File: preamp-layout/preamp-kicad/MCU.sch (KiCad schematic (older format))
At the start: 9 parts, among them J27 Conn_01x04_Female, J29 Conn_01x05_Female, J30 Conn_01x05_Female, J31 Conn_01x05_Female, J32 Conn_01x04_Female, J33 Conn_01x03_Male, J34 Conn_01x02_Male, J35 Conn_01x02_Male, U5 ESP32-DevKitC

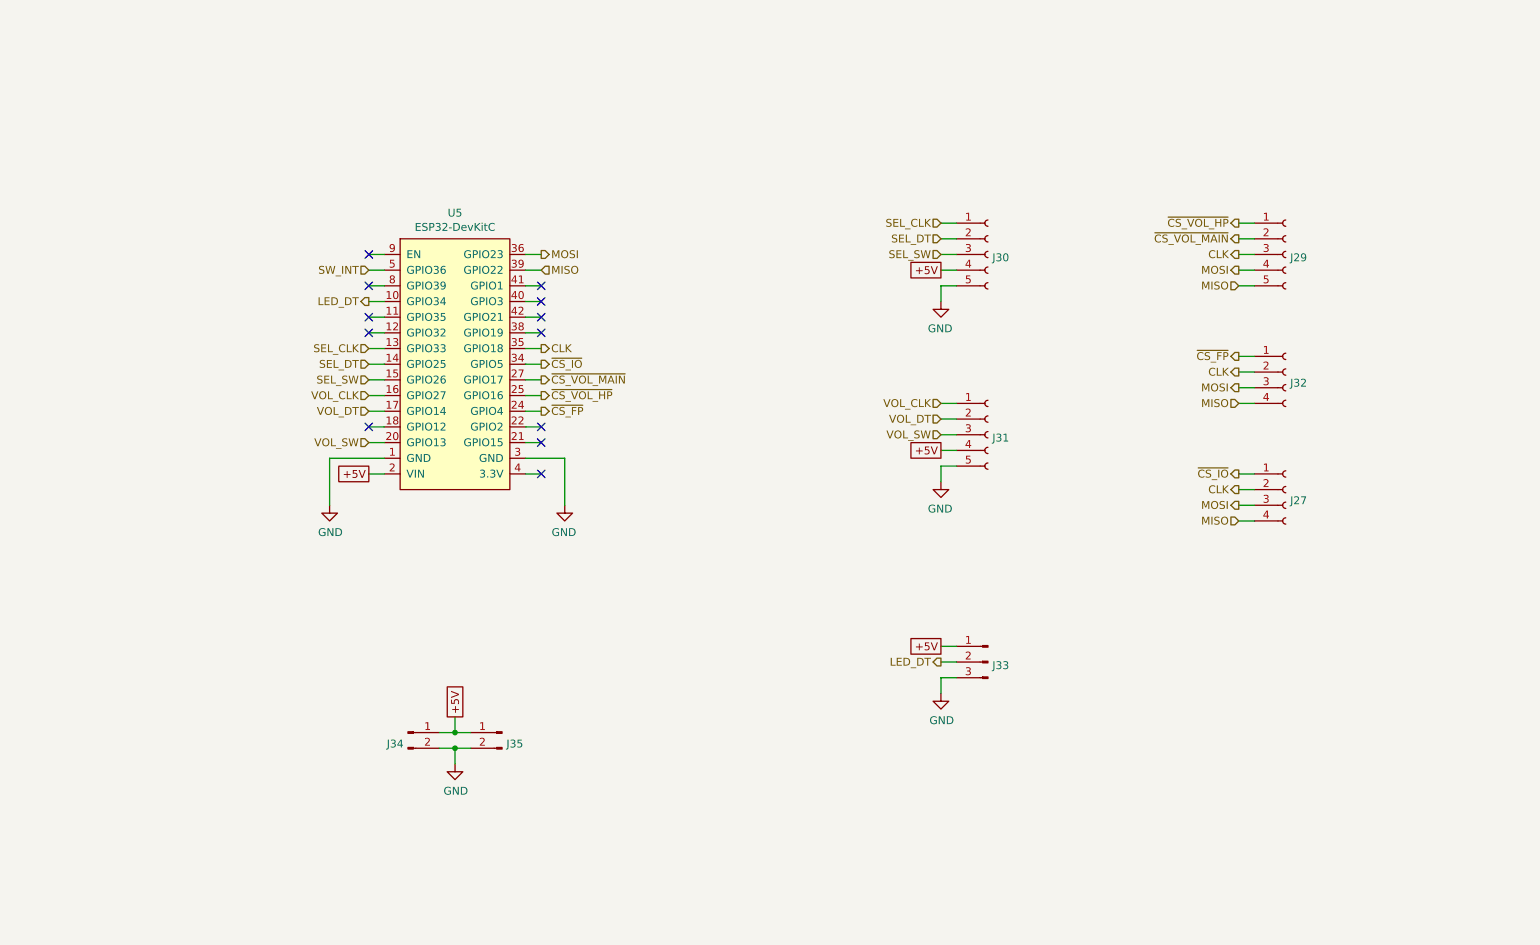
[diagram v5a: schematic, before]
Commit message: I2C init commit
Changed design from using SPI interface to I2C interface, with exception of front LED array (SPI).
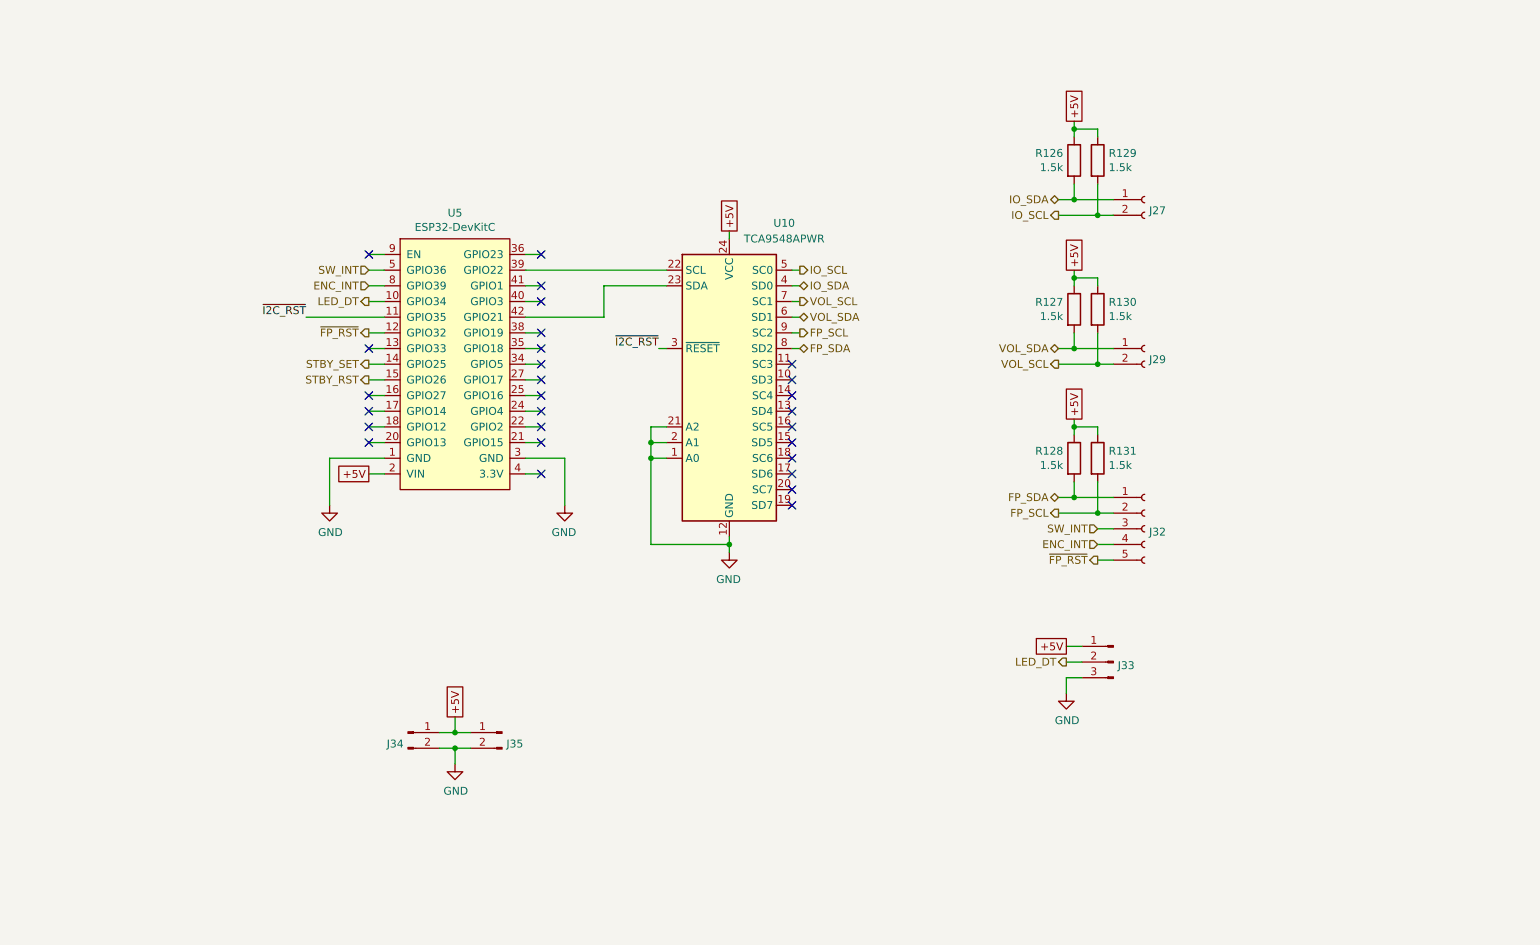
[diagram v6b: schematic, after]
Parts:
- removed J27, J32: Conn_01x04_Female, symbol Connector:Conn_01x04_Female
- removed J29, J30, J31: Conn_01x05_Female, symbol Connector:Conn_01x05_Female
- added J27, J29: Conn_01x02_Female, symbol Connector:Conn_01x02_Female
- added J32: Conn_01x05_Female, symbol Connector:Conn_01x05_Female
- added R126, R127, R128, R129, R130, R131: 1.5k, symbol Device:R
- added U10: TCA9548APWR, Package_SO:TSSOP-24_4.4x7.8mm_P0.65mm, symbol Interface_Expansion:TCA9548APWR
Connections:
- net +5V: now also R126.1, R127.1, R128.1, R129.1, R130.1, R131.1, U10.24 (VCC)
- net GND: now also U10.1 (A0), U10.12 (GND), U10.2 (A1), U10.21 (A2)
- net SW_INT: now also J32.3 (Pin_3)
- net ~I2C_RST: now reaches U5.11 (GPIO35)
- net ~I2C_RST: now also U10.3 (~RESET)
- net ~FP_RST: now reaches U5.12 (GPIO32)
- net ~FP_RST: now also J32.5 (Pin_5)
- net at U5.42 (GPIO21): now also U10.23 (SDA)
- net ENC_INT: now reaches U5.8 (GPIO39)
- net ENC_INT: now also J32.4 (Pin_4)
- net CLK: no longer names the net of U5.35 (GPIO18)
- net MISO: no longer names the net of U5.39 (GPIO22)
- net MISO: now also U10.22 (SCL)
- net MOSI: no longer names the net of U5.36 (GPIO23)
- net SEL_CLK: no longer names the net of U5.13 (GPIO33)
- net SEL_DT renamed STBY_SET
- net SEL_SW renamed STBY_RST
- net VOL_CLK: no longer names the net of U5.16 (GPIO27)
- net VOL_DT: no longer names the net of U5.17 (GPIO14)
- net VOL_SW: no longer names the net of U5.20 (GPIO13)
- net ~CS_FP: no longer names the net of U5.24 (GPIO4)
- net ~CS_IO: no longer names the net of U5.34 (GPIO5)
- net ~CS_VOL_HP: no longer names the net of U5.25 (GPIO16)
- net ~CS_VOL_MAIN: no longer names the net of U5.27 (GPIO17)
- new net FP_SCL: J32.2 (Pin_2), R131.2, U10.9 (SC2)
- new net FP_SDA: J32.1 (Pin_1), R128.2, U10.8 (SD2)
- new net IO_SCL: J27.2 (Pin_2), R129.2, U10.5 (SC0)
- new net IO_SDA: J27.1 (Pin_1), R126.2, U10.4 (SD0)
- new net VOL_SCL: J29.2 (Pin_2), R130.2, U10.7 (SC1)
- new net VOL_SDA: J29.1 (Pin_1), R127.2, U10.6 (SD1)
- no-connect marks 12 -> 28
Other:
- moved on the sheet: J33

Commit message: BOM Update
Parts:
- added J28, J30: Conn_01x15_Female, symbol Connector:Conn_01x15_Female
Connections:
- net +5V: now also J28.15 (Pin_15); no longer U5.2 (VIN)
- net ENC_INT: now also J28.3 (Pin_3); no longer U5.8 (GPIO39)
- net GND: now also J28.14 (Pin_14), J30.14 (Pin_14); no longer U5.1 (GND), U5.3 (GND)
- net LED_DT: now also J28.4 (Pin_4); no longer U5.10 (GPIO34)
- net STBY_RST: now also J28.9 (Pin_9); no longer U5.15 (GPIO26)
- net STBY_SET: now also J28.8 (Pin_8); no longer U5.14 (GPIO25)
- net SW_INT: now also J28.2 (Pin_2); no longer U5.5 (GPIO36)
- net ~FP_RST: now also J28.6 (Pin_6); no longer U5.12 (GPIO32)
- net ~I2C_RST: now also J28.5 (Pin_5); no longer U5.11 (GPIO35)
- net at U10.22 (SCL): now also J30.2 (Pin_2); no longer U5.39 (GPIO22)
- net at U10.23 (SDA): now also J30.5 (Pin_5); no longer U5.42 (GPIO21)
- no-connect marks 28 -> 58
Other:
- moved on the sheet: J27, J29, J32, J33, J34, J35, R126, R127, R128, R129, R130, R131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

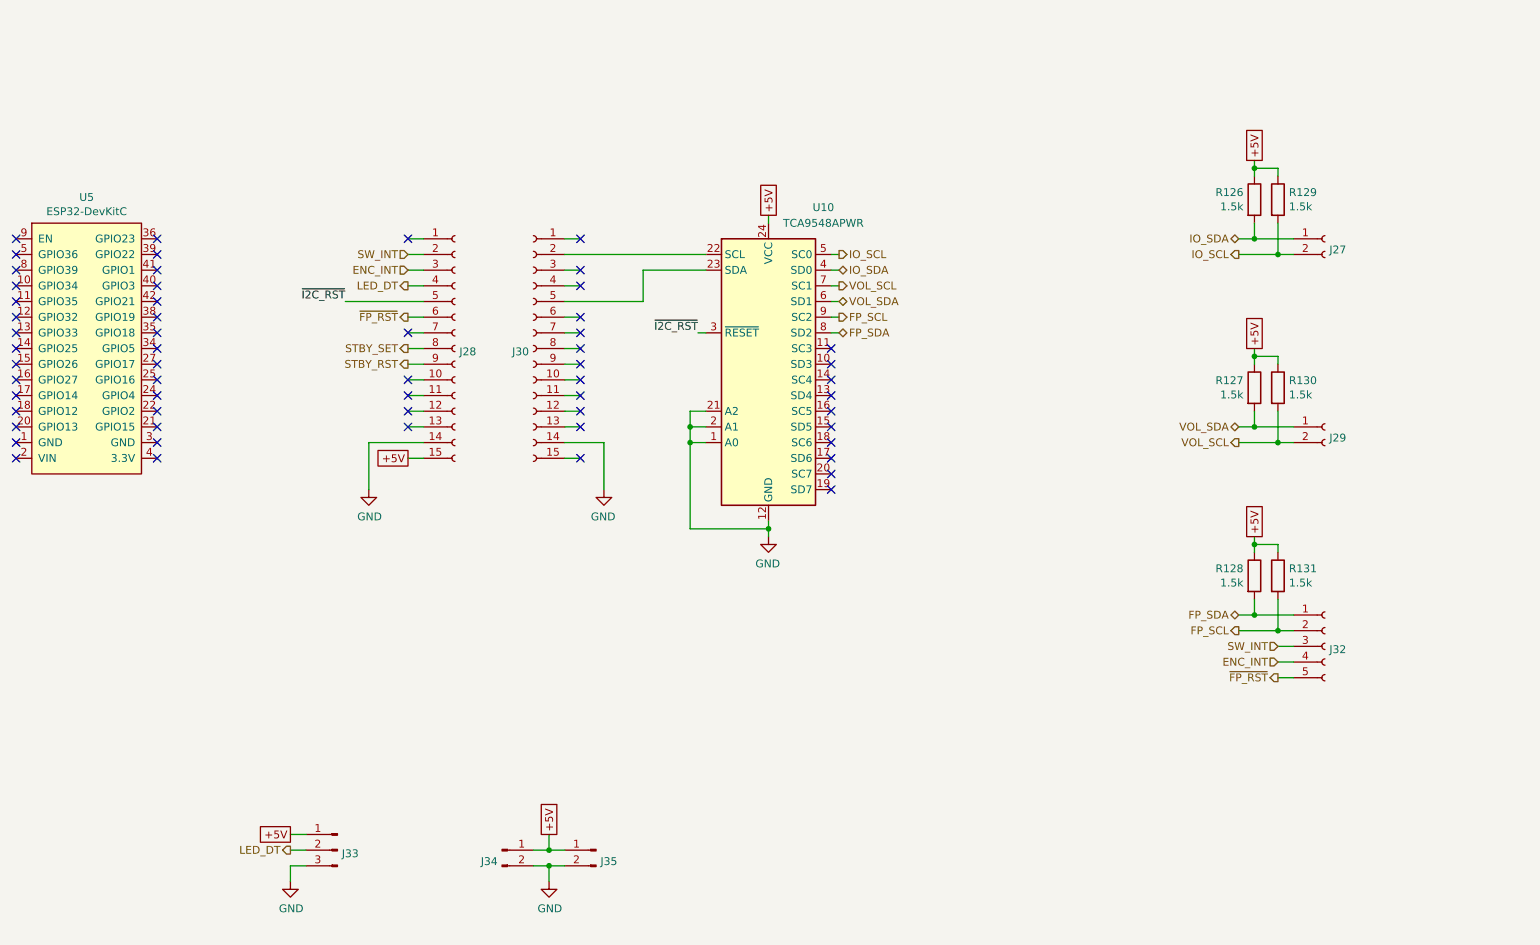
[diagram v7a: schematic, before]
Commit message: woops
to merge with I2C
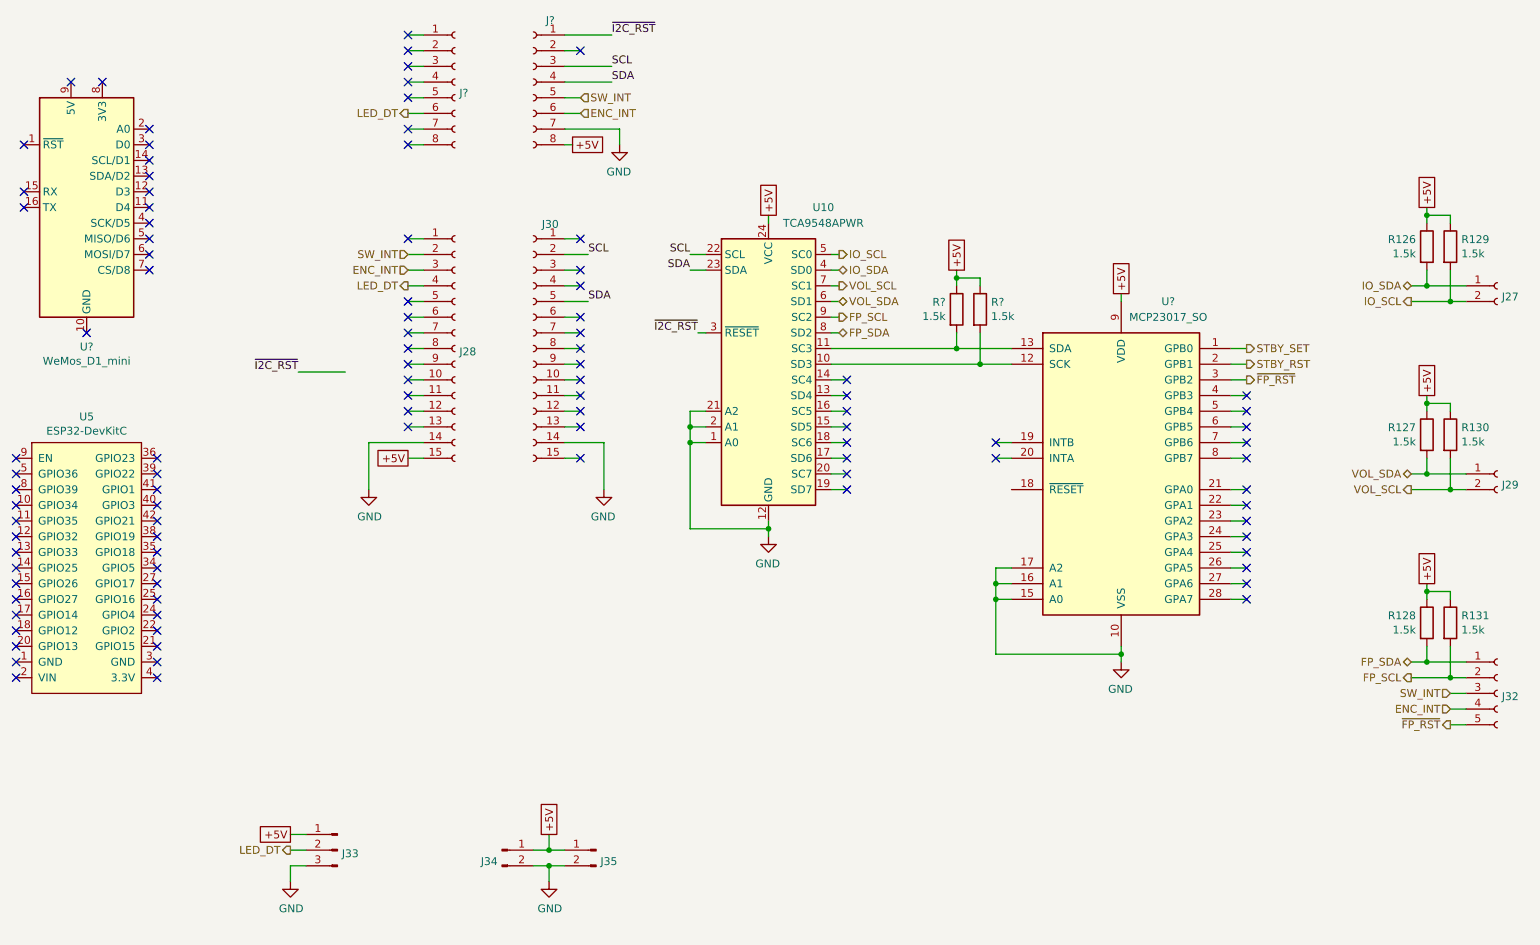
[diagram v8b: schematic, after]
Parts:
- added J? (x2): Conn_01x08_Female, symbol Connector:Conn_01x08_Female
- added R? (x2): 1.5k, symbol Device:R
- added U?: WeMos_D1_mini, Module:WEMOS_D1_mini_light, symbol MCU_Module:WeMos_D1_mini
- added U?: MCP23017_SO, Package_SO:SOIC-28W_7.5x17.9mm_P1.27mm, symbol Interface_Expansion:MCP23017_SO
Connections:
- net +5V: now also J?.8 (Pin_8), R?.1, R?.1, U?.9 (VDD)
- net ENC_INT: now also J?.6 (Pin_6)
- net GND: now also J?.7 (Pin_7), U?.10 (VSS), U?.15 (A0), U?.16 (A1), U?.17 (A2)
- net LED_DT: now also J?.6 (Pin_6)
- net STBY_RST: now also U?.2 (GPB1); no longer J28.9 (Pin_9)
- net STBY_SET: now also U?.1 (GPB0); no longer J28.8 (Pin_8)
- net SW_INT: now also J?.5 (Pin_5)
- net ~FP_RST: now also U?.3 (GPB2); no longer J28.6 (Pin_6)
- net ~I2C_RST: now also J?.1 (Pin_1); no longer J28.5 (Pin_5)
- net SCL: now reaches J30.2 (Pin_2), U10.22 (SCL)
- net SCL: now also J?.3 (Pin_3)
- net SDA: now reaches J30.5 (Pin_5), U10.23 (SDA)
- net SDA: now also J?.4 (Pin_4)
- net at U10.10 (SD3): now also R?.2, U?.12 (SCK)
- net at U10.11 (SC3): now also R?.2, U?.13 (SDA)
- no-connect marks 58 -> 99
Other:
- moved on the sheet: J27, J29, J32, R126, R127, R128, R129, R130, R131, U5
